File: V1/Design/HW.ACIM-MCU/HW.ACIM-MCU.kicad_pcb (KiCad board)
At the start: 4 copper layers, 32 x 20 mm, 17 parts, among them J1 HEADER 2x15POS, J2 HEADER 2x15POS, U1 MIPS 32-bit DSC, U2 12MHz

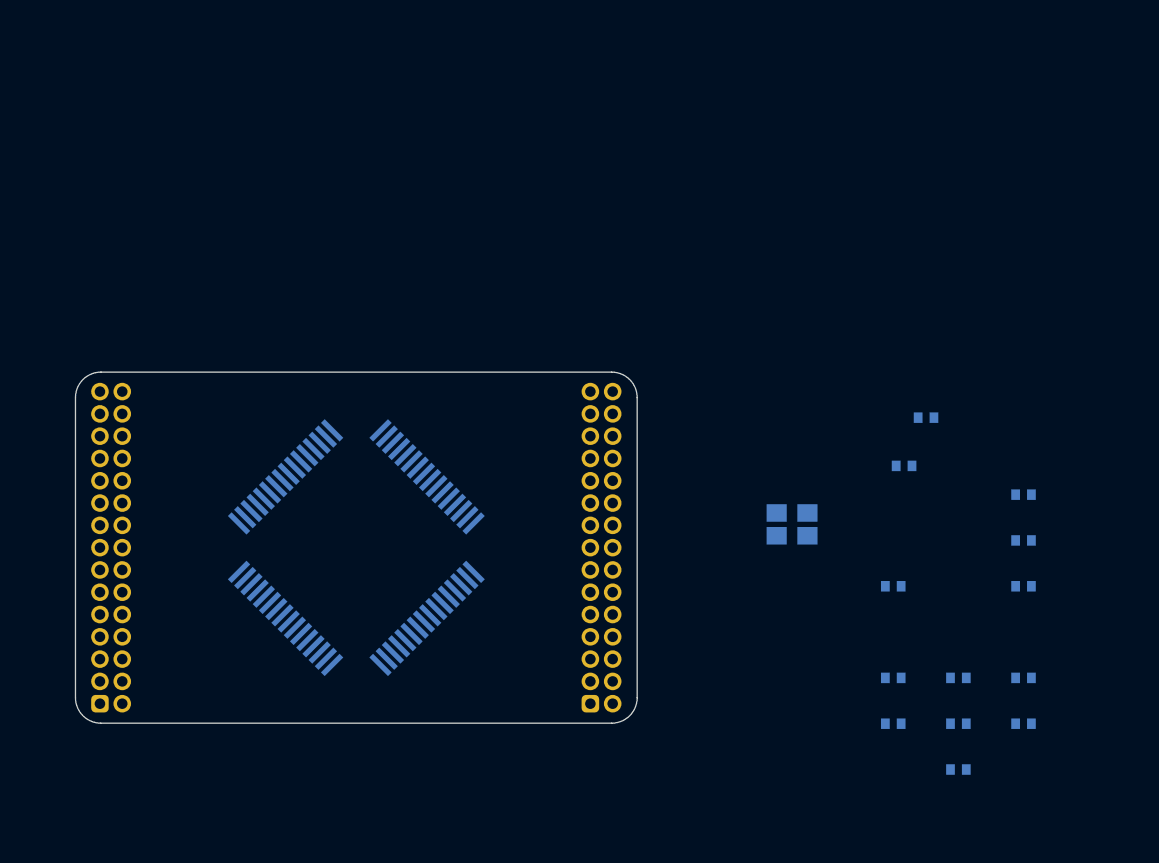
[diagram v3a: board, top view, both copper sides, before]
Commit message: MCU PIM schematic update 6
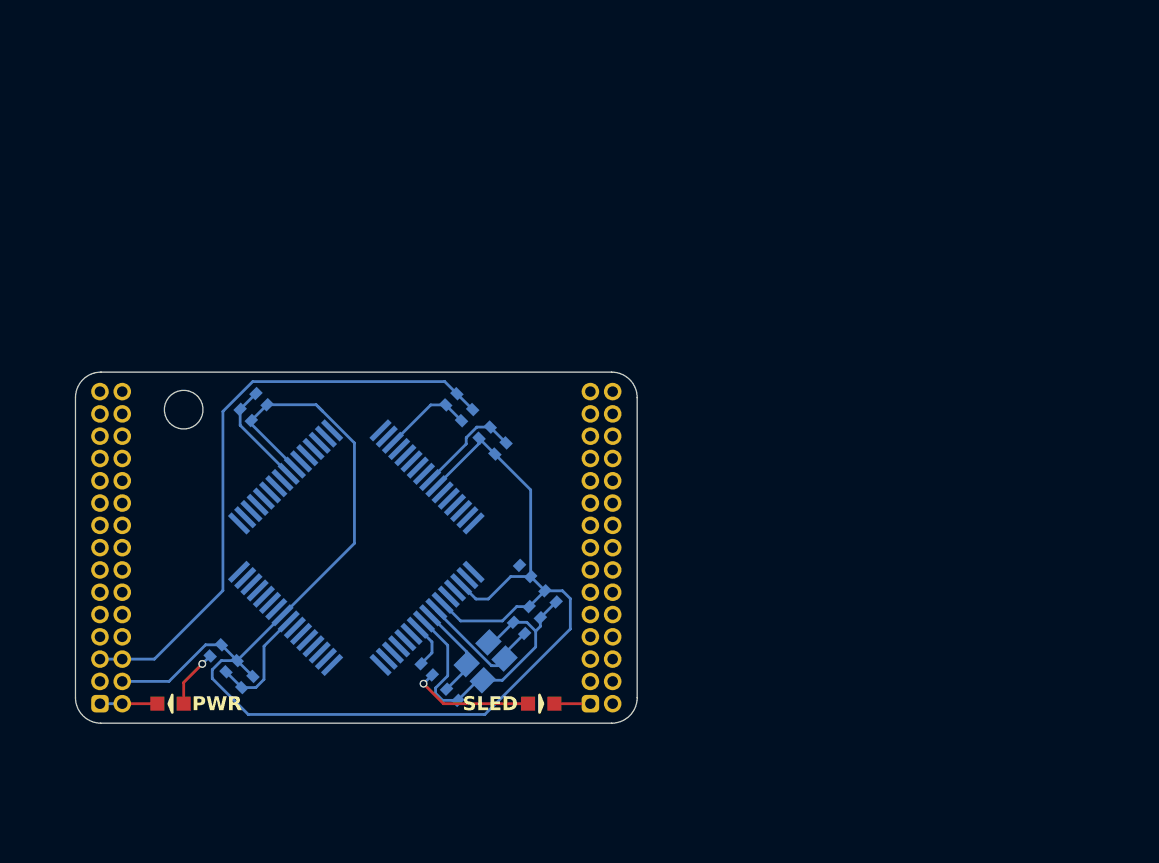
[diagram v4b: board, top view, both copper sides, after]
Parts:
- added D1: SLED, SAMPI:LED0603, F.Cu at (110.9, 111.5)
- added D2: PWR, SAMPI:LED0603, F.Cu at (89.8, 111.5)
- added R1: 1K, SAMPI:RES0402, B.Cu at (104.3, 109.6)
- added R2: 1K, SAMPI:RES0402, B.Cu at (92.3, 108.5)
- added SH1: SCREW HOLDER, SAMPI:HOLDER-2.2MM, F.Cu at (90.5, 94.8)
- moved C27 47.7 mm to (94.0, 95.1), turned to -45 degrees
- moved C22 45.5 mm to (94.1, 110.3), turned to 45 degrees
- moved C21 41.8 mm to (93.2, 109.4), turned to 45 degrees
- moved C28 36.8 mm to (94.9, 94.2), turned to -45 degrees
- moved C26 33.7 mm to (107.6, 96.1), turned to -135 degrees
- moved C13 30.0 mm to (106.6, 95.1), turned to -135 degrees
- moved C12 29.8 mm to (105.7, 94.2), turned to -135 degrees
- moved C20 28.9 mm to (105.8, 111.0), turned to 135 degrees
- moved C24 27.9 mm to (110.5, 106.3), turned to 135 degrees
- moved C23 27.1 mm to (111.4, 105.4), turned to 135 degrees
- moved C19 25.2 mm to (109.6, 107.2), turned to -45 degrees
- moved C25 24.3 mm to (108.5, 97.0), turned to -135 degrees
- moved C10 21.0 mm to (110.0, 104.0), turned to -45 degrees
- moved U2 19.1 mm to (107.7, 109.1), turned to -135 degrees
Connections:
- J1 pad 7: VREF -> AVDD
- J1 pad 8: VREF -> AVDD
- U1 pad 11: /MC_TEMP_SEN -> unconnected-(U1-AN10/CVD10/RPA12/RA12-Pad11)
- U1 pad 12: /PFC_IA -> unconnected-(U1-AN9/CVD9/RPA11/RA11-Pad12)
- U1 pad 13: /PFC_IB -> /MC_IU_SEN
- U1 pad 14: /MC_IU -> /MC_IV_SEN
- U1 pad 15: /MC_IV -> /MC_IW_SEN
- U1 pad 16: /MC_IW -> /MC_VU_DIV
- U1 pad 17: /PGC -> /MC_VV_DIV
- U1 pad 18: /PGD -> /MC_VW_DIV
- U1 pad 2: /GPIO1 -> unconnected-(U1-RPB14/PWM1H/VBUSON1/PMD6/RB14-Pad2)
- U1 pad 21: /MC_VV_DIV -> /PFC_IA_SEN
- U1 pad 22: /MC_VU_DIV -> /PFC_IB_SEN
- U1 pad 23: /MC_VW_DIV -> unconnected-(U1-OA3IN+/AN8/CVD8/C3IN1+/C3IN3-/RPC2/FLT3/PMA13/RC2-Pad23)
- U1 pad 24: /VREF_DIV -> unconnected-(U1-AN11/CVD11/C1IN2-/FLT4/PMA12/RC11-Pad24)
- U1 pad 29: /SDO -> unconnected-(U1-AN14/CVD14/RPE14/FLT7/PMA1/RE14-Pad29)
- U1 pad 3: /GPIO2 -> unconnected-(U1-RPB15/PWM7H/PWM1L/PMD7/RB15-Pad3)
- U1 pad 30: /SDI -> unconnected-(U1-AN15/CVD15/RPE15/FLT8/PMA0/RE15-Pad30)
- U1 pad 31: /SCK -> unconnected-(U1-TDI/DAC3/AN26/CVD26/RPA8/SDA2/PMA9/RA8-Pad31)
- U1 pad 33: /MC_VR_DIV -> /PFC_IDC
- U1 pad 42: unconnected-(U1-RD8-Pad42) -> /SLED
- U1 pad 43: /RXD2 -> /PGC
- U1 pad 44: /RXD1 -> /PGD
- U1 pad 45: /MC_VDC_DIV -> unconnected-(U1-DAC2/AN48/CVD48/RPC10/PMA14/PMCS/RC10-Pad45)
- U1 pad 46: /VAC_DIV -> unconnected-(U1-OA5OUT/AN25/CVD25/C5IN4-/RPB7/SCK1/INT0/RB7-Pad46)
- U1 pad 49: /MC_IDC -> unconnected-(U1-TMS/OA5IN-/AN27/CVD27/LVDIN/C5IN1-/RPB9/RB9-Pad49)
- U1 pad 58: /~{INV_FAULT} -> unconnected-(U1-RPF0/PWM11H/RF0-Pad58)
- U1 pad 59: /~{INV_FLT_OC} -> unconnected-(U1-RPF1/PWM11L/RF1-Pad59)
- U1 pad 60: /PFC_PWM_A -> unconnected-(U1-RPB10/PWM3H/PMD0/RB10-Pad60)
- U1 pad 61: /PFC_PWM_ENA -> unconnected-(U1-RPB11/PWM9H/PWM3L/PMD1/RB11-Pad61)
- U1 pad 62: /PFC_PWM_B -> unconnected-(U1-RPB12/PWM2H/PMD2/RB12-Pad62)
- U1 pad 63: /PFC_PWM_ENB -> unconnected-(U1-RPB13/PWM8H/PWM2L/CTPLS/PMD3/RB13-Pad63)
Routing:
- net +3V3: track 0.00 -> 90.0 mm
- net GND: track 0.00 -> 42.7 mm
- net AGND: track 0.00 -> 34.4 mm
- net Net-(U1-OSCI/CLKI/AN49/CVD49/RPC12/RC12): track 0.00 -> 7.34 mm
- net Net-(D1-PadA): track 0.00 -> 7.14 mm, vias 0 -> 1
- net Net-(U1-OSCO/CLKO/RPC15/RC15): track 0.00 -> 5.55 mm
- net AVDD: track 0.00 -> 5.17 mm
- net Net-(D2-PadA): track 0.00 -> 3.34 mm, vias 0 -> 1
- net /SLED: track 0.00 -> 2.64 mm

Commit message: MCU PIM schematic update 7
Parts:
- removed SH1: SCREW HOLDER, SAMPI:HOLDER-2.2MM
- added C1: 22pF, SAMPI:CAP0402, F.Cu at (87.0, 115.6)
- added R3: 10K, SAMPI:RES0402, F.Cu at (87.0, 117.9)
- C12, C13, C19, C20, C21, C22, C25, C26, C27, C28, R1, R2, U1, U2: moved to F.Cu
- J1, J2: footprint SAMPI:HD-2x15x1.27-TH -> SAMPI:HD-2x15x1.27-SMD
- moved C10 9.31 mm to (104.1, 111.2), turned to 135 degrees
- moved R1 7.89 mm to (112.0, 111.5), turned to 180 degrees
- moved C23 6.94 mm to (105.8, 109.5)
- moved C24 6.87 mm to (104.9, 110.4)
- moved C19 6.78 mm to (104.2, 111.4)
- moved R2 5.56 mm to (90.8, 113.9)
- moved C28 4.80 mm to (97.7, 90.3)
- moved C27 4.80 mm to (93.3, 90.4)
- moved C13 4.53 mm to (108.3, 90.9)
- moved C21 4.35 mm to (93.4, 113.8)
- moved C20 4.06 mm to (108.0, 107.6)
- moved C22 3.98 mm to (95.5, 114.1)
- moved D1 3.61 mm to (114.5, 111.5)
- moved C25 3.50 mm to (105.3, 95.6)
- moved C12 3.14 mm to (105.2, 91.1)
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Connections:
- net /ENC_INDEX renamed /ENC_IDX
- net /MC_VDC_DIV renamed /IDC_SEN
- J1 pad 1: GND -> AGND
- J1 pad 10: /IO3 -> unconnected-(J1-Pad10)
- J1 pad 11: /IO0 -> unconnected-(J1-Pad11)
- J1 pad 12: /IO1 -> unconnected-(J1-Pad12)
- J1 pad 13: /~{CS} -> unconnected-(J1-Pad13)
- J1 pad 14: /SDI -> unconnected-(J1-Pad14)
- J1 pad 15: /SDO -> unconnected-(J1-Pad15)
- J1 pad 16: /SCK -> unconnected-(J1-Pad16)
- J1 pad 2: GND -> AGND
- J1 pad 21: /PFC_IA_SEN -> /VAC_DIV
- J1 pad 23: /VAC_DIV -> /VDC_DIV
- J1 pad 26: /MC_IDC_SEN -> /PFC_IA_SEN
- J1 pad 3: +3V3 -> AVDD
- J1 pad 4: +3V3 -> AVDD
- J1 pad 5: AGND -> unconnected-(J1-Pad5)
- J1 pad 6: AGND -> unconnected-(J1-Pad6)
- J1 pad 7: AVDD -> unconnected-(J1-Pad7)
- J1 pad 8: AVDD -> unconnected-(J1-Pad8)
- J1 pad 9: /IO2 -> unconnected-(J1-Pad9)
- J2 pad 1: GND -> /VBUS
- J2 pad 10: /TXD1 -> /TXD2
- J2 pad 11: /RXD2 -> unconnected-(J2-Pad11)
- J2 pad 12: /TXD2 -> unconnected-(J2-Pad12)
- J2 pad 13: /IND_ERR -> unconnected-(J2-Pad13)
- J2 pad 14: /IND_RUN -> unconnected-(J2-Pad14)
- J2 pad 15: /MC_PWM_WL -> /~{INV_FLT}
- J2 pad 16: /MC_PWM_WH -> unconnected-(J2-Pad16)
- J2 pad 17: /MC_PWM_VL -> /MC_PWM_WH
- J2 pad 18: /MC_PWM_VH -> /MC_PWM_WL
- J2 pad 19: /MC_PWM_UL -> /MC_PWM_VH
- J2 pad 20: /MC_PWM_UH -> /MC_PWM_VL
- J2 pad 21: /~{INV_FLT} -> /MC_PWM_UH
- J2 pad 22: /MC_VR_DIV -> /MC_PWM_UL
- J2 pad 23: /VREF_DIV -> /MC_VR_DIV
- J2 pad 24: /MC_TEMP_SEN -> /MC_IU_SEN
- J2 pad 25: /MC_IU_SEN -> /MC_TEMP_SEN
- J2 pad 26: /MC_VW_DIV -> /MC_IV_SEN
- J2 pad 27: /MC_IV_SEN -> +3V3
- J2 pad 28: /MC_VV_DIV -> +3V3
- J2 pad 29: /MC_IW_SEN -> GND
- J2 pad 3: /USB_P -> /USB_N
- J2 pad 30: /MC_VU_DIV -> GND
- J2 pad 5: /USB_N -> /USB_P
- J2 pad 7: /VBUS -> /RXD1
- J2 pad 8: /~{BT_UBT} -> /TXD1
- J2 pad 9: /RXD1 -> /RXD2
- U1 pad 13: /MC_IU_SEN -> unconnected-(U1-OA2OUT/AN0/C2IN4-/C4IN3-/RPA0/RA0-Pad13)
- U1 pad 14: /MC_IV_SEN -> unconnected-(U1-OA2IN+/AN1/C2IN1+/RPA1/RA1-Pad14)
- U1 pad 15: /MC_IW_SEN -> unconnected-(U1-PGD3/VREF-/OA2IN-/AN2/C2IN1-/RPB0/CTED2/RB0-Pad15)
- U1 pad 16: /MC_VU_DIV -> unconnected-(U1-PGC3/OA1OUT/VREF+/AN3/C1IN4-/C4IN2-/RPB1/CTED1/RB1-Pad16)
- U1 pad 17: /MC_VV_DIV -> unconnected-(U1-PGC1/OA1IN+/AN4/C1IN1+/C1IN3-/C2IN3-/RPB2/RB2-Pad17)
- U1 pad 18: /MC_VW_DIV -> unconnected-(U1-PGD1/OA1IN-/AN5/CTCMP/C1IN1-/RTCC/RPB3/RB3-Pad18)
- U1 pad 30: unconnected-(U1-AN15/CVD15/RPE15/FLT8/PMA0/RE15-Pad30) -> /MC_VR_DIV
- U1 pad 31: unconnected-(U1-TDI/DAC3/AN26/CVD26/RPA8/SDA2/PMA9/RA8-Pad31) -> /MC_IV_SEN
- U1 pad 33: /PFC_IDC -> /MC_IU_SEN
- U1 pad 43: /PGC -> /PGD
- U1 pad 44: /PGD -> /PGC
- U1 pad 45: unconnected-(U1-DAC2/AN48/CVD48/RPC10/PMA14/PMCS/RC10-Pad45) -> /TXD2
- U1 pad 46: unconnected-(U1-OA5OUT/AN25/CVD25/C5IN4-/RPB7/SCK1/INT0/RB7-Pad46) -> /TXD1
- U1 pad 47: unconnected-(U1-SOSCI/RPC13/RC13-Pad47) -> /RXD1
- U1 pad 48: unconnected-(U1-SOSCO/T1CK/RPB8/RB8-Pad48) -> /RXD2
- U1 pad 49: unconnected-(U1-TMS/OA5IN-/AN27/CVD27/LVDIN/C5IN1-/RPB9/RB9-Pad49) -> /MC_TEMP_SEN
- U1 pad 59: unconnected-(U1-RPF1/PWM11L/RF1-Pad59) -> /~{INV_FLT}
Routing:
- net +3V3: track 90.0 -> 11.5 mm, vias 0 -> 4
- net GND: track 42.7 -> 4.11 mm, vias 0 -> 2
- net AGND: track 34.4 -> 0.00 mm
- net /MC_IU_SEN: track 0.00 -> 24.0 mm, vias 0 -> 2
- net /~{MCLR}: track 0.00 -> 22.1 mm, vias 0 -> 2
- net /MC_IV_SEN: track 0.00 -> 21.6 mm, vias 0 -> 2
- net /MC_VR_DIV: track 0.00 -> 19.8 mm, vias 0 -> 2
- net /PGD: track 0.00 -> 12.9 mm, vias 0 -> 1
- net /MC_PWM_VL: track 0.00 -> 12.4 mm, vias 0 -> 1
- net /TXD2: track 0.00 -> 12.4 mm, vias 0 -> 2
- net /PGC: track 0.00 -> 12.1 mm, vias 0 -> 1
- net /VBUS: track 0.00 -> 12.0 mm, vias 0 -> 2
- net /USB_N: track 0.00 -> 11.5 mm, vias 0 -> 1
- net /USB_P: track 0.00 -> 11.2 mm, vias 0 -> 1
- net /~{INV_FLT}: track 0.00 -> 9.95 mm, vias 0 -> 1
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- added copper zone on B.Cu, net GND
- added copper zone on F.Cu, net GND
- added copper zone on In1.Cu, net GND
- added copper zone on In2.Cu, net GND

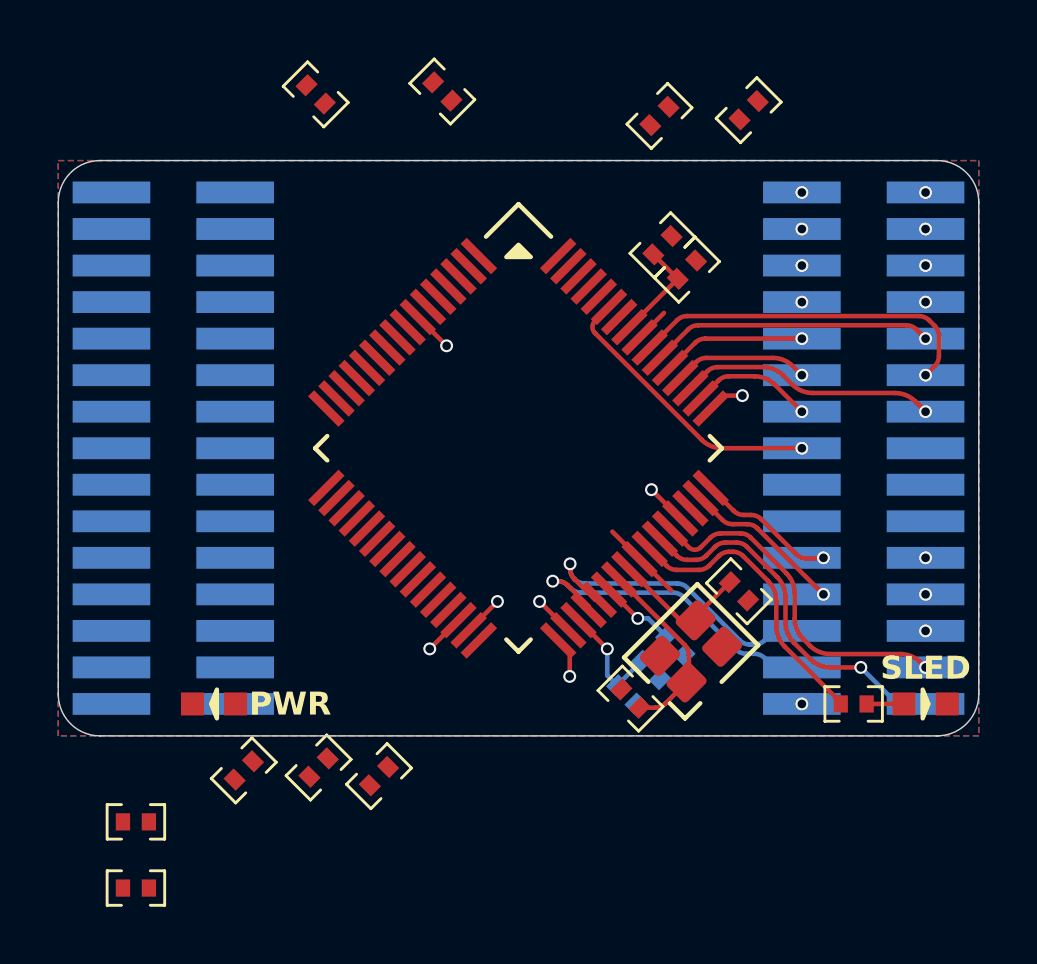
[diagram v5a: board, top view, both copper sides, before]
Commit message: MCU PIM schematic update 8
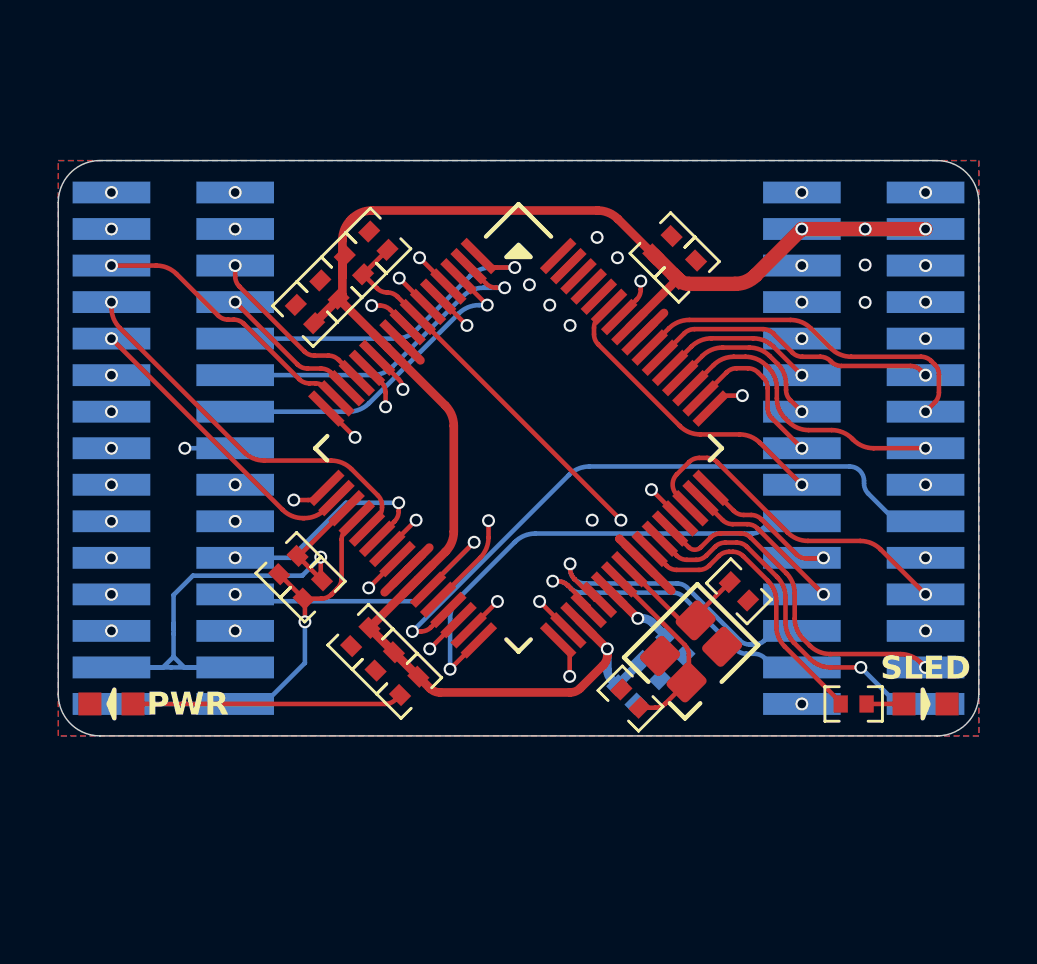
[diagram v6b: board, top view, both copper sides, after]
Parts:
- moved R3 22.9 mm to (94.6, 96.3), turned to 135 degrees
- moved C13 22.5 mm to (92.3, 106.7), turned to 45 degrees
- moved C1 21.9 mm to (95.5, 95.4), turned to -45 degrees
- moved C12 20.4 mm to (93.2, 107.6), turned to 45 degrees
- moved C28 9.09 mm to (92.9, 98.0)
- moved C27 6.80 mm to (93.8, 97.1)
- moved R2 6.46 mm to (96.5, 110.9)
- moved C22 4.88 mm to (94.8, 109.2)
- moved C21 4.35 mm to (95.7, 110.1)
- moved D2 3.56 mm to (86.2, 111.5)
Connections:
- J1 pad 10: unconnected-(J1-Pad10) -> /IO04
- J1 pad 11: unconnected-(J1-Pad11) -> /IO05
- J1 pad 12: unconnected-(J1-Pad12) -> /IO06
- J1 pad 13: unconnected-(J1-Pad13) -> /IO07
- J1 pad 14: unconnected-(J1-Pad14) -> /IO08
- J1 pad 15: unconnected-(J1-Pad15) -> /IO09
- J1 pad 16: unconnected-(J1-Pad16) -> /IO10
- J1 pad 5: unconnected-(J1-Pad5) -> GND
- J1 pad 6: unconnected-(J1-Pad6) -> GND
- J1 pad 7: unconnected-(J1-Pad7) -> /IO01
- J1 pad 8: unconnected-(J1-Pad8) -> /IO02
- J1 pad 9: unconnected-(J1-Pad9) -> /IO03
- J2 pad 11: unconnected-(J2-Pad11) -> /RTS2
- J2 pad 12: unconnected-(J2-Pad12) -> /CTS2
- J2 pad 13: unconnected-(J2-Pad13) -> /~{INV_FLT}
- J2 pad 14: unconnected-(J2-Pad14) -> /IO00
- J2 pad 15: /~{INV_FLT} -> /MC_PWM_WH
- J2 pad 16: unconnected-(J2-Pad16) -> /MC_PWM_WL
- J2 pad 17: /MC_PWM_WH -> /MC_PWM_VH
- J2 pad 18: /MC_PWM_WL -> /MC_PWM_VL
- J2 pad 19: /MC_PWM_VH -> /MC_PWM_UH
- J2 pad 20: /MC_PWM_VL -> /MC_PWM_UL
- J2 pad 21: /MC_PWM_UH -> /MC_TEMP_SEN
- J2 pad 22: /MC_PWM_UL -> /MC_VR_DIV
- J2 pad 23: /MC_VR_DIV -> /MC_VU_DIV
- J2 pad 25: /MC_TEMP_SEN -> /MC_VV_DIV
- U1 pad 1: unconnected-(U1-TCK/RPA7/PWM10H/PWM4L/PMD5/RA7-Pad1) -> /~{PFC_FLT}
- U1 pad 11: unconnected-(U1-AN10/CVD10/RPA12/RA12-Pad11) -> /PFC_PWM_ENA
- U1 pad 12: unconnected-(U1-AN9/CVD9/RPA11/RA11-Pad12) -> /PFC_PWM_ENB
- U1 pad 13: unconnected-(U1-OA2OUT/AN0/C2IN4-/C4IN3-/RPA0/RA0-Pad13) -> /PFC_IA_SEN
- U1 pad 14: unconnected-(U1-OA2IN+/AN1/C2IN1+/RPA1/RA1-Pad14) -> /PFC_IB_SEN
- U1 pad 15: unconnected-(U1-PGD3/VREF-/OA2IN-/AN2/C2IN1-/RPB0/CTED2/RB0-Pad15) -> /IDC_SEN
- U1 pad 16: unconnected-(U1-PGC3/OA1OUT/VREF+/AN3/C1IN4-/C4IN2-/RPB1/CTED1/RB1-Pad16) -> /MC_VU_DIV
- U1 pad 17: unconnected-(U1-PGC1/OA1IN+/AN4/C1IN1+/C1IN3-/C2IN3-/RPB2/RB2-Pad17) -> /IO09
- U1 pad 18: unconnected-(U1-PGD1/OA1IN-/AN5/CTCMP/C1IN1-/RTCC/RPB3/RB3-Pad18) -> /VAC_DIV
- U1 pad 2: unconnected-(U1-RPB14/PWM1H/VBUSON1/PMD6/RB14-Pad2) -> /PFC_PWM_A
- U1 pad 21: /PFC_IA_SEN -> /VDC_DIV
- U1 pad 22: /PFC_IB_SEN -> /IO04
- U1 pad 23: unconnected-(U1-OA3IN+/AN8/CVD8/C3IN1+/C3IN3-/RPC2/FLT3/PMA13/RC2-Pad23) -> /MC_VV_DIV
- U1 pad 24: unconnected-(U1-AN11/CVD11/C1IN2-/FLT4/PMA12/RC11-Pad24) -> /IO03
- U1 pad 27: unconnected-(U1-AN12/CVD12/C2IN2-/C5IN2-/SDA4/FLT5/PMA11/RE12-Pad27) -> /IO02
- U1 pad 28: unconnected-(U1-AN13/CVD13/C3IN2-/FLT6/SCL4/PMA10/RE13-Pad28) -> /IO01
- U1 pad 29: unconnected-(U1-AN14/CVD14/RPE14/FLT7/PMA1/RE14-Pad29) -> /CTS2
- U1 pad 3: unconnected-(U1-RPB15/PWM7H/PWM1L/PMD7/RB15-Pad3) -> /PFC_PWM_B
- U1 pad 32: unconnected-(U1-FLT15/RPB4/SCL2/PMA8/RB4-Pad32) -> /RTS2
- U1 pad 58: unconnected-(U1-RPF0/PWM11H/RF0-Pad58) -> /IO00
- U1 pad 60: unconnected-(U1-RPB10/PWM3H/PMD0/RB10-Pad60) -> /IO08
- U1 pad 61: unconnected-(U1-RPB11/PWM9H/PWM3L/PMD1/RB11-Pad61) -> /IO07
- U1 pad 62: unconnected-(U1-RPB12/PWM2H/PMD2/RB12-Pad62) -> /IO06
- U1 pad 63: unconnected-(U1-RPB13/PWM8H/PWM2L/CTPLS/PMD3/RB13-Pad63) -> /IO05
- U1 pad 64: unconnected-(U1-TDO/PWM4H/PMD4/RA10-Pad64) -> /IO10
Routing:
- net +3V3: track 11.5 -> 65.4 mm, vias 4 -> 5
- net /CTS2: track 0.00 -> 22.7 mm, vias 0 -> 1
- net AVDD: track 0.00 -> 21.3 mm, vias 0 -> 1
- net /MC_VV_DIV: track 0.00 -> 19.9 mm, vias 0 -> 2
- net /MC_VU_DIV: track 0.00 -> 18.8 mm, vias 0 -> 2
- net /IO01: track 0.00 -> 18.5 mm, vias 0 -> 2
- net /IO00: track 0.00 -> 17.5 mm, vias 0 -> 2
- net /RTS2: track 0.00 -> 17.0 mm, vias 0 -> 1
- net /ENC_IDX: track 0.00 -> 15.4 mm, vias 0 -> 2
- net AGND: track 0.00 -> 14.7 mm, vias 0 -> 1
- net /VDC_DIV: track 0.00 -> 13.6 mm, vias 0 -> 1
- net /ENC_B: track 0.00 -> 12.5 mm, vias 0 -> 2
- net /TXD1: track 0.00 -> 12.1 mm
- net /PFC_PWM_A: track 0.00 -> 12.1 mm, vias 0 -> 1
- net /~{PFC_FLT}: track 0.00 -> 12.0 mm, vias 0 -> 1
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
